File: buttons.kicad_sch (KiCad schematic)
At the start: 16 parts, among them SW1 DTSM32N, SW2 DTSM32N, SW3 DTSM32N, SW4 DTSM32N

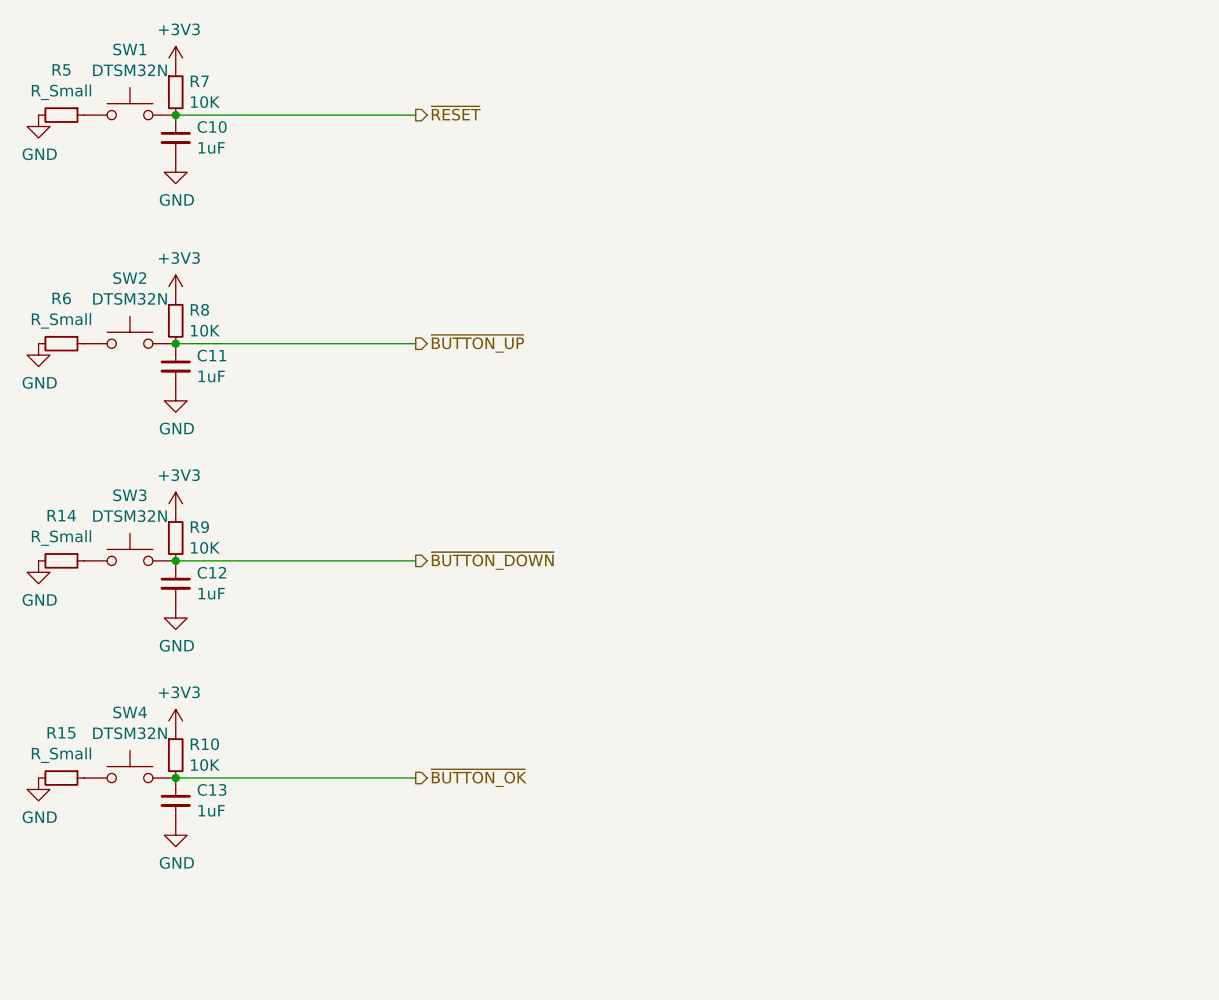
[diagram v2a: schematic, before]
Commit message: Clean buttons schematic
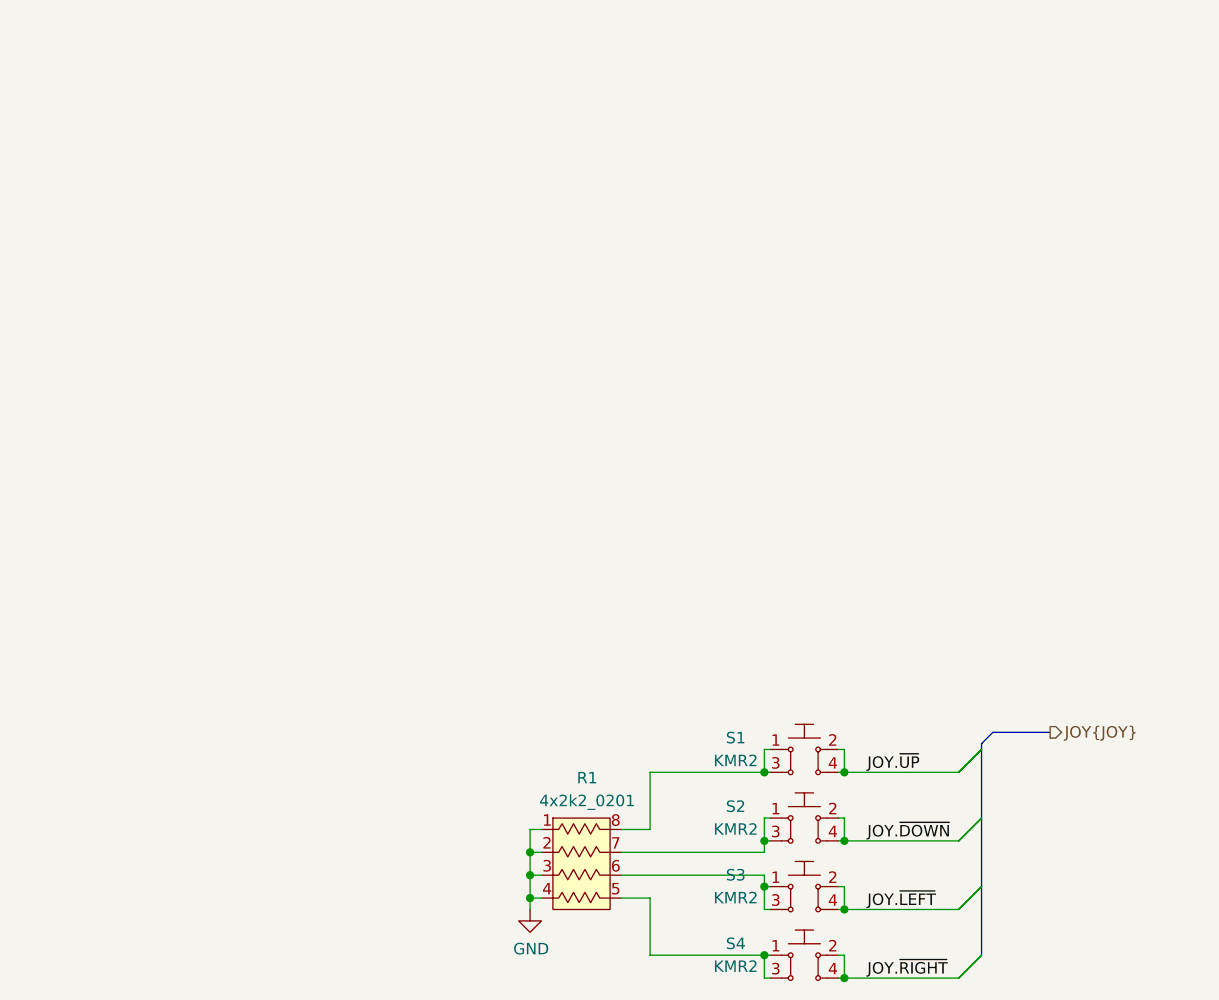
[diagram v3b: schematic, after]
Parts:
- removed C10, C11, C12, C13: 1uF, Capacitor_SMD:C_0402_1005Metric, symbol Device:C_Small
- removed R10, R7, R8, R9: 10K, Resistor_SMD:R_0402_1005Metric, symbol Device:R_Small
- removed R14, R15, R5, R6: R_Small, Resistor_SMD:R_0402_1005Metric, symbol Device:R_Small
- removed SW1, SW2, SW3, SW4: DTSM32N, Button_Switch_SMD:SW_SPST_B3U-1000P, symbol Switch:SW_Push
- added R1: 4x10k_0201_array, antmicro-footprints:EXB18V, symbol antmicroResistorNetworksArrays:4x10k_0201_array
- added S1, S2, S3, S4: KMR2, antmicro-footprints:SW_SPST_4.2x2.8, symbol antmicroPushbuttonSwitches:KMR2
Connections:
- net GND: now also R1.1, R1.2, R1.3, R1.4
- new net: R1.6, S3.1, S3.3
- new net: R1.8, S1.1, S1.3
- new net: R1.7, S2.1, S2.3
- new net: R1.5, S4.1, S4.3
- new net JOY.~{DOWN}: S2.2, S2.4
- new net JOY.~{LEFT}: S3.2, S3.4
- new net JOY.~{RIGHT}: S4.2, S4.4
- new net JOY.~{UP}: S1.2, S1.4

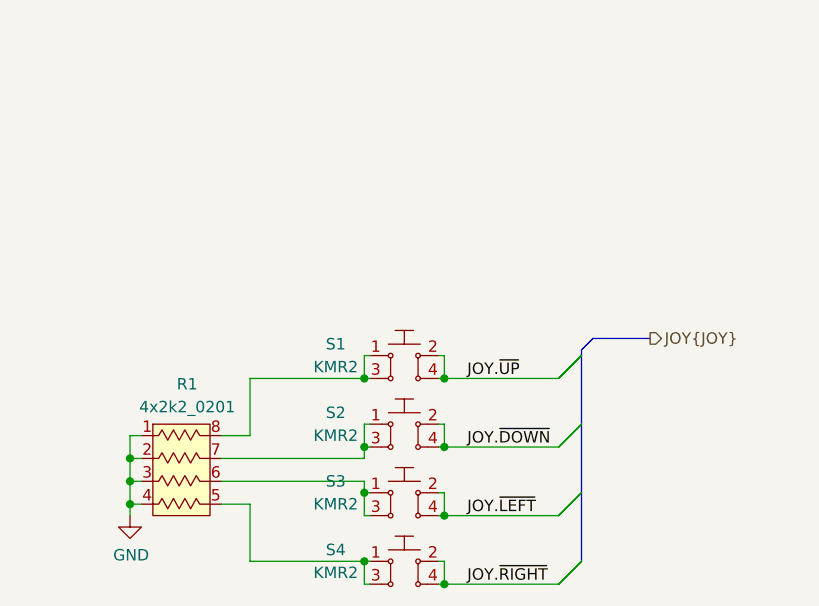
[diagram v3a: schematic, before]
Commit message: Replace buttons with minature joystick
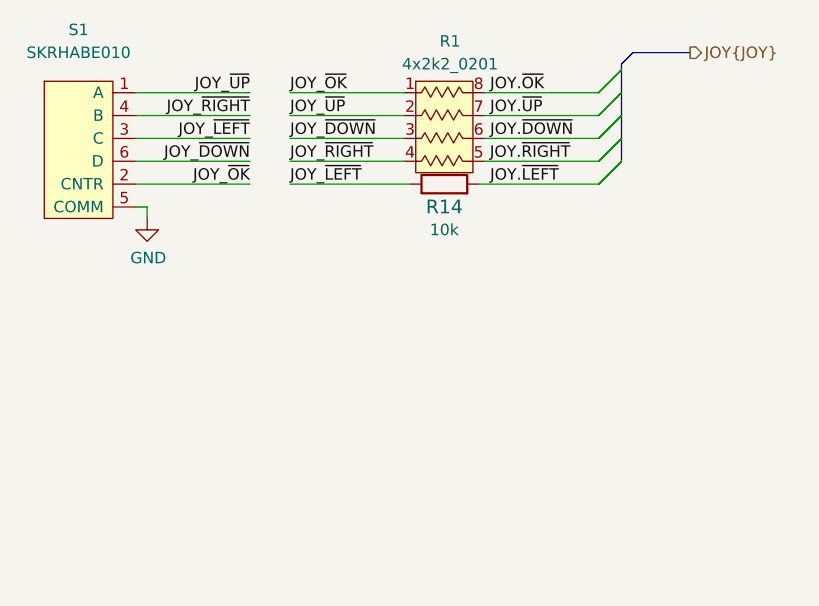
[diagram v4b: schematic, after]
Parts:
- removed S1, S2, S3, S4: KMR2, antmicro-footprints:SW_SPST_4.2x2.8, symbol antmicroPushbuttonSwitches:KMR2
- added R14: R_10k_0402, antmicro-footprints:0402-res, symbol antmicroResistors0402:R_10k_0402
- added S1: SKRHABE010, antmicro-footprints:SKRHABE010, symbol antmicroPushbuttonSwitches:SKRHABE010
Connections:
- net GND: now also S1.5 (COMM); no longer R1.1, R1.2, R1.3, R1.4
- net JOY.~{DOWN}: now also R1.6
- net JOY.~{LEFT}: now also R14.2
- net JOY.~{RIGHT}: now also R1.5
- net JOY.~{UP}: now also R1.7
- net JOY.~{OK}: now reaches R1.8
- new net JOY_~{DOWN}: R1.3, S1.6 (D)
- new net JOY_~{LEFT}: R14.1, S1.3 (C)
- new net JOY_~{OK}: R1.1, S1.2 (CNTR)
- new net JOY_~{RIGHT}: R1.4, S1.4 (B)
- new net JOY_~{UP}: R1.2, S1.1 (A)
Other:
- moved on the sheet: R1

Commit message: Loclib, cleanup
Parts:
- R1: footprint antmicro-footprints:EXB18V -> synermycha-electronics-footprints:EXB18V; symbol antmicroResistorNetworksArrays:4x10k_0201_array -> synermycha-electronics:4x10k_0201_array
- R14: footprint antmicro-footprints:0402-res -> synermycha-electronics-footprints:0402-res; symbol antmicroResistors0402:R_10k_0402 -> synermycha-electronics:R_10k_0402
- S1: footprint antmicro-footprints:SKRHABE010 -> synermycha-electronics-footprints:SKRHABE010; symbol antmicroPushbuttonSwitches:SKRHABE010 -> synermycha-electronics:SKRHABE010
